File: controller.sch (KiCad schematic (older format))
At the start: 26 parts, among them J1 CONN_01X04, J2 CONN_01X02, J3 CONN_01X02, J4 CONN_01X02, J5 CONN_01X02, J6 CONN_01X02, U1 ATTINY13A-SU

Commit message: Make last changes
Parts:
- removed J4, J5: CONN_01X02, Connectors:PINHEAD1-2, symbol CONN_01X02
- added D4: D, symbol D
- added Q1: BF244A, TO_SOT_Packages_THT:TO-92_Molded_Narrow, symbol BF244A
- added Q?: IRLB8721PBF, TO_SOT_Packages_THT:TO-220_Vertical, symbol IRLB8721PBF
- added U2: TL072, symbol TL072
- C1: value 47uF -> 220u
- C6: value 220uF -> 470u
- R1, R3: value 220 -> 1K
- R5: value 3.3K -> 4.3K
- R6: value 1K -> 1.2K
- R7: value 10K -> 1K; footprint Resistors_SMD:R_1206 -> (none)
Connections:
- net +2V8: now also D4.1 (K), Q1.1 (D), Q?.3 (S); no longer C1.1, C2.1, DC1.4 (VIN), J3.2 (P2), L1.2
- net +5V: now also U2.8 (V+), U2.8 (V+)
- net GND: now also D1.1 (K), D2.1 (K), Q?.1 (G), U2.4 (V-), U2.4 (V-); no longer R1.2, R3.2, R7.1
- net miso: now also J6.2 (P2)
- net at R7.2, U1.2 (PB3(CLKI/ADC3/PCINT3)): no longer DC1.2 (EN)
- net at R1.1: now also D1.2 (A); no longer D1.1 (K)
- net at R3.1: now also D2.2 (A); no longer D2.1 (K)
- net mosi renamed RC
- net RC: now also U2.3 (+)
- net sck renamed GC
- net GC: now also U2.5 (+); no longer J6.2 (P2)
- new net: R1.2, U2.1, U2.2 (-)
- new net: R3.2, U2.6 (-), U2.7
- new net: Q1.2 (G), R7.1
- new net VCC: C1.1, C2.1, DC1.4 (VIN), L1.2, Q1.3 (S)
- new net VDD: D4.2 (A), J3.2 (P2), Q?.2 (D)
- no-connect marks 0 -> 1
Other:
- moved on the sheet: D1, D2, R1

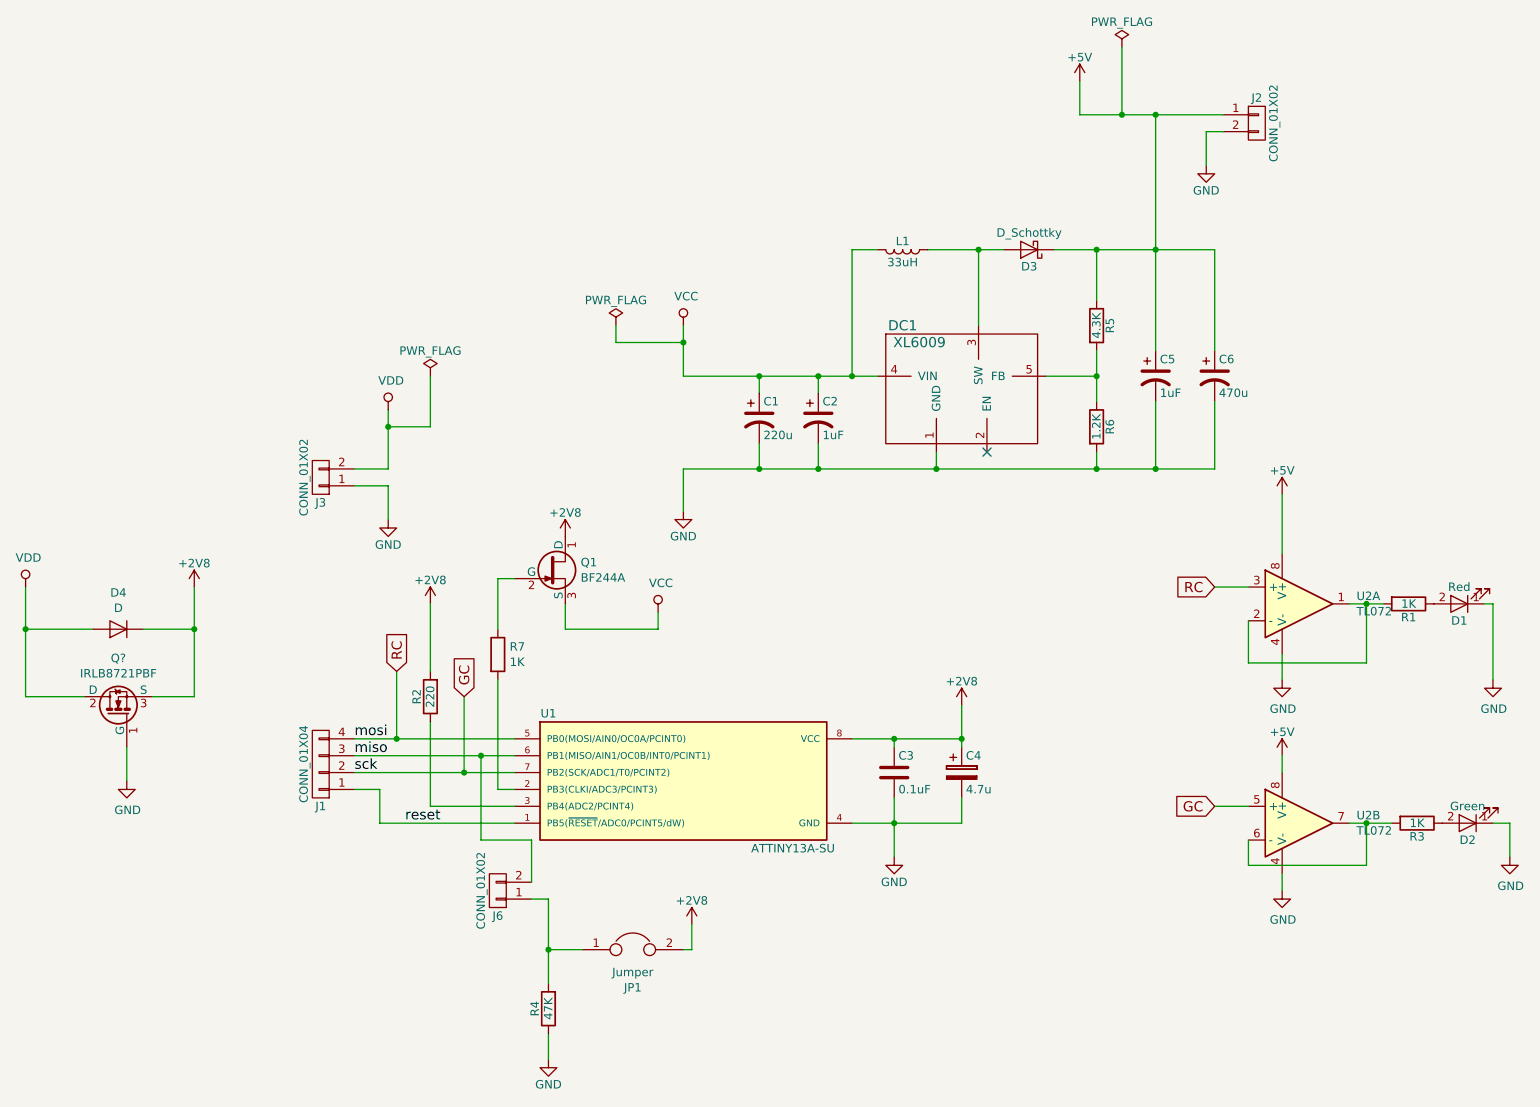
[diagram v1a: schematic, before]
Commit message: add circuit protection, refactor
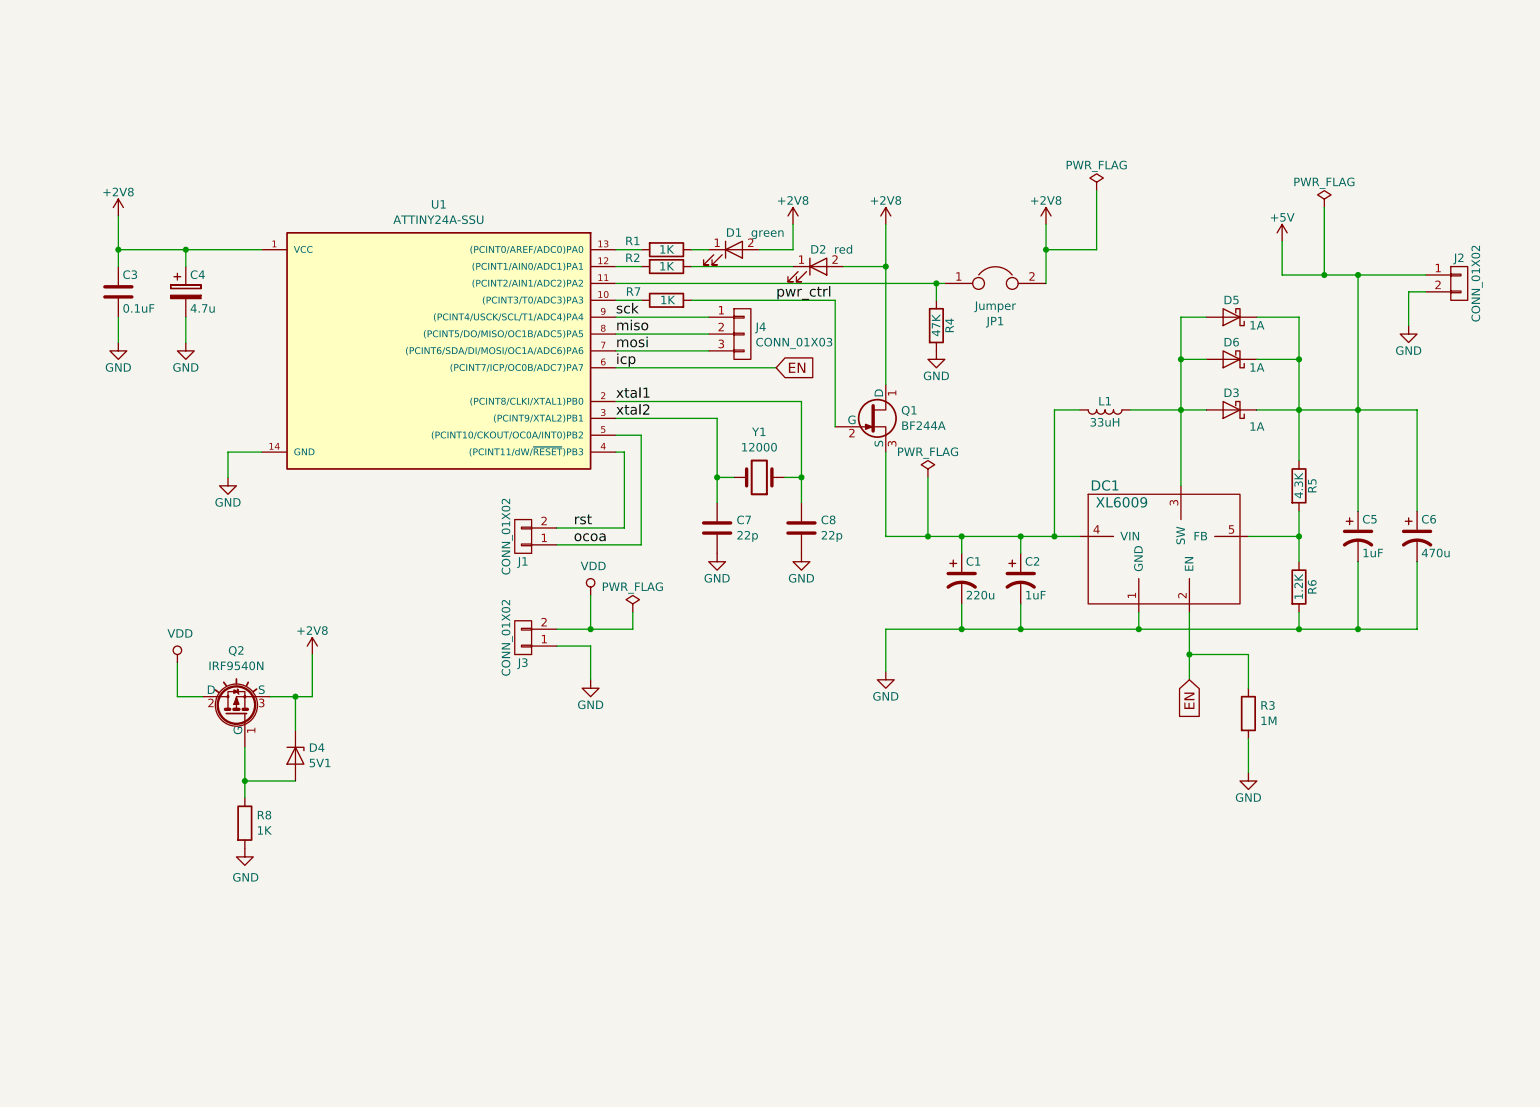
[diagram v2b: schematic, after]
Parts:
- removed D4: D, symbol D
- removed J1: CONN_01X04, Connectors_Molex:Molex_KK-6410-04_04x2.54mm_Straight, symbol CONN_01X04
- removed J6: CONN_01X02, Connectors:PINHEAD1-2, symbol CONN_01X02
- removed Q?: IRLB8721PBF, TO_SOT_Packages_THT:TO-220_Vertical, symbol IRLB8721PBF
- removed U1: ATTINY13A-SU, SMD_Packages:SOIC-8-N, symbol ATTINY13A-SU
- removed U2: TL072, symbol TL072
- added C7, C8: 22p, symbol C
- added D4: 5V1, symbol D_Zener_SOT23
- added D5, D6: 1A, Diodes_THT:D_DO-201_P12.70mm_Horizontal, symbol D_Schottky
- added J1: CONN_01X02, Connectors:PINHEAD1-2, symbol CONN_01X02
- added J4: CONN_01X03, symbol CONN_01X03
- added Q2: IRF9540N, TO_SOT_Packages_THT:TO-220_Vertical, symbol IRF9540N
- added R8: 1K, symbol R
- added U1: ATTINY24A-SSU, Housings_SOIC:SOIC-14_3.9x8.7mm_Pitch1.27mm, symbol ATTINY24A-SSU
- added Y1: 12000, symbol Crystal
- D1: value Red -> green
- D2: value Green -> red
- D3: value D_Schottky -> 1A
- R2: value 220 -> 1K
- R3: value 1K -> 1M; footprint Resistors_SMD:R_1206 -> (none)
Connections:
- net +2V8: now also D1.2 (A), D2.2 (A), D4.3 (K), Q2.3 (S), U1.1 (VCC); no longer R2.2
- net +5V: now also D5.1 (K), D6.1 (K)
- net GND: now also R3.2, R4.2, C7.2, C8.2, R8.2, U1.14 (GND); no longer D1.1 (K), D2.1 (K), R4.1
- net VDD: now also Q2.2 (D)
- net miso: now also J4.2 (P2), U1.8 ((PCINT5/DO/MISO/OC1B/ADC5)PA5)
- net EN: now reaches DC1.2 (EN)
- net EN: now also R3.1, U1.6 ((PCINT7/ICP/OC0B/ADC7)PA7)
- net at D3.2 (A), DC1.3 (SW), L1.1: now also D5.2 (A), D6.2 (A)
- net at R1.1: now also D1.1 (K); no longer D1.2 (A)
- net at R1.2: now also U1.13 ((PCINT0/AREF/ADC0)PA0)
- net pwr_ctrl: now reaches R7.2
- net pwr_ctrl: now also Q1.2 (G)
- net at R2.1: now also D2.1 (K)
- net at JP1.1: now also R4.1, U1.11 ((PCINT2/AIN1/ADC2)PA2); no longer R4.2
- net at R7.1: now also U1.10 ((PCINT3/T0/ADC3)PA3); no longer Q1.2 (G)
- net VCC: no longer names the net of C1.1, C2.1, DC1.4 (VIN), L1.2, Q1.3 (S)
- new net: R2.2, U1.12 ((PCINT1/AIN0/ADC1)PA1)
- new net: D4.1 (A), Q2.1 (G), R8.1
- new net mosi: J4.3 (P3), U1.7 ((PCINT6/SDA/DI/MOSI/OC1A/ADC6)PA6)
- new net ocoa: J1.1 (P1), U1.5 ((PCINT10/CKOUT/OC0A/INT0)PB2)
- new net rst: J1.2 (P2), U1.4 ((PCINT11/dW/~RESET~)PB3)
- new net sck: J4.1 (P1), U1.9 ((PCINT4/USCK/SCL/T1/ADC4)PA4)
- new net xtal1: C8.1, U1.2 ((PCINT8/CLKI/XTAL1)PB0), Y1.1
- new net xtal2: C7.1, U1.3 ((PCINT9/XTAL2)PB1), Y1.2
- no-connect marks 1 -> 0
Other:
- moved on the sheet: C1, C2, C4, C5, C6, D1, D3, DC1, J2, J3, L1, Q1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

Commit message: Remove ocsillators, add aref connection and pin for voltage check
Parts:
- removed C8: 22p, symbol C
- removed Y1: 12000, symbol Crystal
- added R9: 670K, Resistors_SMD:R_1206, symbol R
- C7: value 22p -> C
- J1: footprint Connectors:PINHEAD1-2 -> (none)
- J4: value CONN_01X03 -> SPI
- R3: footprint (none) -> Resistors_SMD:R_1206
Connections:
- net xtal1 is gone; now on an unnamed net: U1.2 ((PCINT8/CLKI/XTAL1)PB0)
- net +2V8: now also U1.12 ((PCINT1/AIN0/ADC1)PA1), R9.1
- net GND: now also C7.1, R9.2; no longer C7.2
- net at R1.2: now also U1.3 ((PCINT9/XTAL2)PB1); no longer U1.13 ((PCINT0/AREF/ADC0)PA0)
- net at R2.2: no longer U1.12 ((PCINT1/AIN0/ADC1)PA1)
- net ocoa: no longer names the net of J1.1 (P1), U1.5 ((PCINT10/CKOUT/OC0A/INT0)PB2)
- removed net xtal2: C7.1, U1.3 ((PCINT9/XTAL2)PB1)
- new net: C7.2, U1.13 ((PCINT0/AREF/ADC0)PA0)
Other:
- moved on the sheet: D1, D2, J3, R1, R2

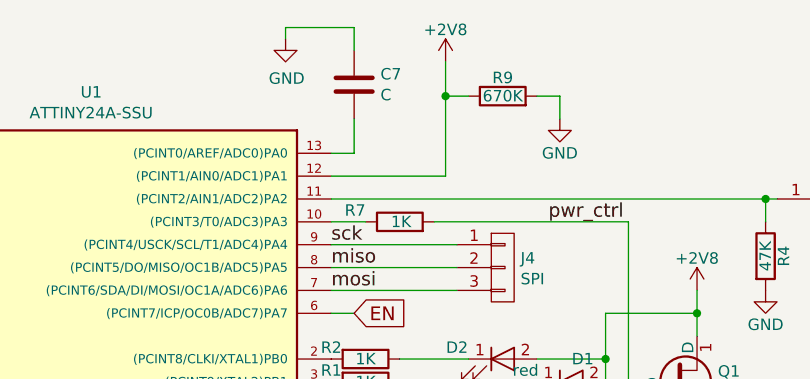
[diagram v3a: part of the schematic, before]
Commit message: Add capacitor value
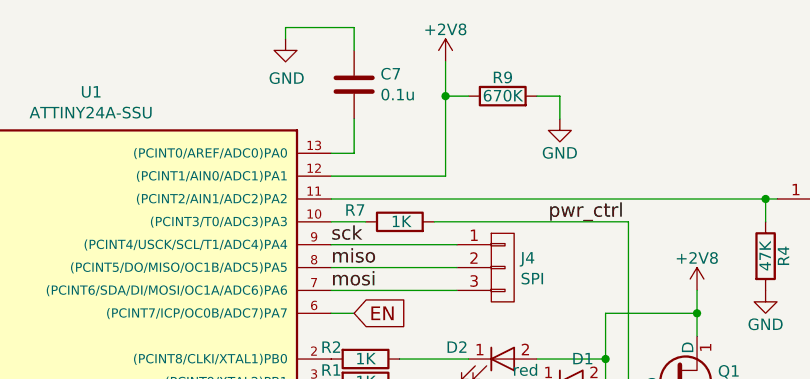
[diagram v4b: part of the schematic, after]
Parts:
- C7: value C -> 0.1u
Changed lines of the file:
@@
 Connection ~ 9350 3050
 $Comp
-L GND #PWR14
+L GND #PWR01
 U 1 1 58F22530
 P 6550 4600
-F 0 "#PWR14" H 6550 4350 50  0001 C CNN
+F 0 "#PWR01" H 6550 4350 50  0001 C CNN
 F 1 "GND" H 6550 4450 50  0000 C CNN
 F 2 "" H 6550 4600 50  0001 C CNN
@@
 	8900 2250 9750 2250
 $Comp
-L +5V #PWR18
+L +5V #PWR02
 U 1 1 58F23334
 P 8900 2050
-F 0 "#PWR18" H 8900 1900 50  0001 C CNN
+F 0 "#PWR02" H 8900 1900 50  0001 C CNN
 F 1 "+5V" H 8900 2190 50  0000 C CNN
 F 2 "" H 8900 2050 50  0001 C CNN
@@
 Connection ~ 9350 2250
 $Comp
-L GND #PWR19
+L GND #PWR03
 U 1 1 58F23494
 P 9650 2550
-F 0 "#PWR19" H 9650 2300 50  0001 C CNN
+F 0 "#PWR03" H 9650 2300 50  0001 C CNN
 F 1 "GND" H 9650 2400 50  0000 C CNN
 F 2 "" H 9650 2550 50  0001 C CNN
@@
 Connection ~ 8050 4350
 $Comp
-L PWR_FLAG #FLG4
+L PWR_FLAG #FLG04
 U 1 1 58F2B1AC
 P 9150 1850
-F 0 "#FLG4" H 9150 1925 50  0001 C CNN
+F 0 "#FLG04" H 9150 1925 50  0001 C CNN
 F 1 "PWR_FLAG" H 9150 2000 50  0000 C CNN
 F 2 "" H 9150 1850 50  0001 C CNN
@@
 	4050 5000 4500 5000
 $Comp
-L GND #PWR9
+L GND #PWR05
 U 1 1 58F2DC5B
 P 4250 5300
-F 0 "#PWR9" H 4250 5050 50  0001 C CNN
+F 0 "#PWR05" H 4250 5050 50  0001 C CNN
 F 1 "GND" H 4250 5150 50  0000 C CNN
 F 2 "" H 4250 5300 50  0001 C CNN
@@
 $EndComp
 $Comp
-L +2V8 #PWR16
+L +2V8 #PWR06
 U 1 1 592B3D9B
 P 7500 1950
-F 0 "#PWR16" H 7500 1800 50  0001 C CNN
+F 0 "#PWR06" H 7500 1800 50  0001 C CNN
 F 1 "+2V8" H 7500 2090 50  0000 C CNN
 F 2 "" H 7500 1950 50  0001 C CNN
@@
 $EndComp
 $Comp
-L PWR_FLAG #FLG2
+L PWR_FLAG #FLG07
 U 1 1 592D3FE0
 P 4500 4900
-F 0 "#FLG2" H 4500 4975 50  0001 C CNN
+F 0 "#FLG07" H 4500 4975 50  0001 C CNN
 F 1 "PWR_FLAG" H 4500 5050 50  0000 C CNN
 F 2 "" H 4500 4900 50  0001 C CNN
@@
 $EndComp
 $Comp
-L +2V8 #PWR7
+L +2V8 #PWR08
 U 1 1 592D4CFB
 P 3150 4500
-F 0 "#PWR7" H 3150 4350 50  0001 C CNN
+F 0 "#PWR08" H 3150 4350 50  0001 C CNN
 F 1 "+2V8" H 3150 4640 50  0000 C CNN
 F 2 "" H 3150 4500 50  0001 C CNN
@@
 $EndComp
 $Comp
-L GND #PWR6
+L GND #PWR09
 U 1 1 592D55AC
 P 2750 5650
-F 0 "#PWR6" H 2750 5400 50  0001 C CNN
+F 0 "#PWR09" H 2750 5400 50  0001 C CNN
 F 1 "GND" H 2755 5477 50  0000 C CNN
 F 2 "" H 2750 5650 50  0001 C CNN
@@
 $EndComp
 $Comp
-L VDD #PWR8
+L VDD #PWR010
 U 1 1 592D58A6
 P 4250 4800
-F 0 "#PWR8" H 4250 4650 50  0001 C CNN
+F 0 "#PWR010" H 4250 4650 50  0001 C CNN
 F 1 "VDD" H 4267 4973 50  0000 C CNN
 F 2 "" H 4250 4800 50  0001 C CNN
@@
 $EndComp
 $Comp
-L VDD #PWR3
+L VDD #PWR011
 U 1 1 592D5D4B
 P 2350 4550
-F 0 "#PWR3" H 2350 4400 50  0001 C CNN
+F 0 "#PWR011" H 2350 4400 50  0001 C CNN
 F 1 "VDD" H 2367 4723 50  0000 C CNN
 F 2 "" H 2350 4550 50  0001 C CNN
@@
 	2000 2100 2850 2100
 $Comp
-L GND #PWR5
+L GND #PWR012
 U 1 1 5932EF34
 P 2650 3450
-F 0 "#PWR5" H 2650 3200 50  0001 C CNN
+F 0 "#PWR012" H 2650 3200 50  0001 C CNN
 F 1 "GND" H 2650 3300 50  0000 C CNN
 F 2 "" H 2650 3450 50  0001 C CNN
@@
 $EndComp
 $Comp
-L +2V8 #PWR13
+L +2V8 #PWR013
 U 1 1 593325FC
 P 6550 2700
-F 0 "#PWR13" H 6550 2550 50  0001 C CNN
+F 0 "#PWR013" H 6550 2550 50  0001 C CNN
 F 1 "+2V8" H 6550 2840 50  0000 C CNN
 F 2 "" H 6550 2700 50  0001 C CNN
@@
 $EndComp
 $Comp
-L GND #PWR15
+L GND #PWR014
 U 1 1 5933473B
 P 6850 2700
-F 0 "#PWR15" H 6850 2450 50  0001 C CNN
+F 0 "#PWR014" H 6850 2450 50  0001 C CNN
 F 1 "GND" H 6850 2550 50  0000 C CNN
 F 2 "" H 6850 2700 50  0001 C CNN
@@
 $EndComp
 $Comp
-L +2V8 #PWR1
+L +2V8 #PWR015
 U 1 1 59341595
 P 2000 1900
-F 0 "#PWR1" H 2000 1750 50  0001 C CNN
+F 0 "#PWR015" H 2000 1750 50  0001 C CNN
 F 1 "+2V8" H 2000 2040 50  0000 C CNN
 F 2 "" H 2000 1900 50  0001 C CNN
@@
 Connection ~ 2000 2100
 $Comp
-L GND #PWR2
+L GND #PWR016
 U 1 1 59341A81
 P 2000 2650
-F 0 "#PWR2" H 2000 2400 50  0001 C CNN
+F 0 "#PWR016" H 2000 2400 50  0001 C CNN
 F 1 "GND" H 2000 2500 50  0000 C CNN
 F 2 "" H 2000 2650 50  0001 C CNN
@@
 $EndComp
 $Comp
-L GND #PWR4
+L GND #PWR017
 U 1 1 59341C3E
 P 2400 2650
-F 0 "#PWR4" H 2400 2400 50  0001 C CNN
+F 0 "#PWR017" H 2400 2400 50  0001 C CNN
 F 1 "GND" H 2400 2500 50  0000 C CNN
 F 2 "" H 2400 2650 50  0001 C CNN
@@
 $EndComp
 $Comp
-L GND #PWR17
+L GND #PWR018
 U 1 1 59343DED
 P 8700 5200
-F 0 "#PWR17" H 8700 4950 50  0001 C CNN
+F 0 "#PWR018" H 8700 4950 50  0001 C CNN
 F 1 "GND" H 8700 5050 50  0000 C CNN
 F 2 "" H 8700 5200 50  0001 C CNN
@@
 	6550 3300 6550 3800
 $Comp
-L PWR_FLAG #FLG3
+L PWR_FLAG #FLG019
 U 1 1 593471A3
 P 6800 3450
-F 0 "#FLG3" H 6800 3525 50  0001 C CNN
+F 0 "#FLG019" H 6800 3525 50  0001 C CNN
 F 1 "PWR_FLAG" H 6800 3600 50  0000 C CNN
 F 2 "" H 6800 3450 50  0001 C CNN
@@
 rst
 $Comp
-L +2V8 #PWR11
+L +2V8 #PWR020
 U 1 1 593C5363
 P 5450 1700
-F 0 "#PWR11" H 5450 1550 50  0001 C CNN
+F 0 "#PWR020" H 5450 1550 50  0001 C CNN
 F 1 "+2V8" H 5450 1840 50  0000 C CNN
 F 2 "" H 5450 1700 50  0001 C CNN
@@
 $EndComp
 $Comp
-L GND #PWR12
+L GND #PWR021
 U 1 1 593C5E5C
 P 5950 1950
-F 0 "#PWR12" H 5950 1700 50  0001 C CNN
+F 0 "#PWR021" H 5950 1700 50  0001 C CNN
 F 1 "GND" H 5950 1800 50  0000 C CNN
 F 2 "" H 5950 1950 50  0001 C CNN
@@
 $EndComp
 $Comp
-L PWR_FLAG #FLG1
+L PWR_FLAG #FLG022
 U 1 1 593CBD3E
 P 3450 4250
-F 0 "#FLG1" H 3450 4325 50  0001 C CNN
+F 0 "#FLG022" H 3450 4325 50  0001 C CNN
 F 1 "PWR_FLAG" H 3450 4400 50  0000 C CNN
 F 2 "" H 3450 4250 50  0001 C CNN
@@
 P 5050 1800
 F 0 "C7" H 5165 1846 50  0000 L CNN
-F 1 "C" H 5165 1755 50  0000 L CNN
+F 1 "0.1u" H 5165 1755 50  0000 L CNN
 F 2 "" H 5088 1650 50  0001 C CNN
 F 3 "" H 5050 1800 50  0001 C CNN
@@
 $EndComp
 $Comp
-L GND #PWR10
+L GND #PWR023
 U 1 1 593CEE71
 P 4750 1600
-F 0 "#PWR10" H 4750 1350 50  0001 C CNN
+F 0 "#PWR023" H 4750 1350 50  0001 C CNN
 F 1 "GND" H 4755 1427 50  0000 C CNN
 F 2 "" H 4750 1600 50  0001 C CNN

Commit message: Save changes
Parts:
- removed D5, D6: 1A, Diodes_THT:D_DO-201_P12.70mm_Horizontal, symbol D_Schottky
- added C8: 220u, Capacitors_SMD:CP_Elec_5x5.3, symbol CP1
- added C9: 470u, Capacitors_Tantalum_SMD:CP_Tantalum_Case-V_EIA-7343-20_Hand, symbol CP1
- added R10: 1.5K, Resistors_SMD:R_1206, symbol R
- C2, C5: footprint Capacitors_SMD:C_1210 -> Capacitors_SMD:C_0805
- C7: footprint (none) -> Capacitors_SMD:C_0805
- D3: value 1A -> 5A
- J1: footprint (none) -> Connectors_Molex:Molex_KK-6410-02_02x2.54mm_Straight
- J2, J3: footprint Connectors:PINHEAD1-2 -> Connectors_Molex:Molex_KK-6410-02_02x2.54mm_Straight
- J4: footprint (none) -> Connectors_Molex:Molex_KK-6410-03_03x2.54mm_Straight
- R1, R2: value 1K -> 330
- R5: value 4.3K -> 3.6K
- R7, R8: footprint (none) -> Resistors_SMD:R_1206
- R9: value 670K -> 330
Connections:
- net +2V8: now also R10.1; no longer D1.2 (A), D2.2 (A), R9.1, U1.12 ((PCINT1/AIN0/ADC1)PA1)
- net +5V: now also C9.1
- net GND: now also R1.2, R2.2, C8.2, C9.2
- net at C1.1, C2.1, DC1.4 (VIN)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: now also C8.1
- net at U1.3 ((PCINT9/XTAL2)PB1): now also D2.2 (A); no longer R1.2
- net at U1.2 ((PCINT8/CLKI/XTAL1)PB0): now also D1.2 (A); no longer R2.2
- net ss: now reaches J1.1 (P1), U1.5 ((PCINT10/CKOUT/OC0A/INT0)PB2)
- new net: R10.2, R9.1, U1.12 ((PCINT1/AIN0/ADC1)PA1)
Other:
- moved on the sheet: D1, D2, R1, R2

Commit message: save changes
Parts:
- removed Q1: BF244A, TO_SOT_Packages_THT:TO-92_Molded_Narrow, symbol BF244A
- removed Q2: IRF9540N, TO_SOT_Packages_THT:TO-220_Vertical, symbol IRF9540N
- added Q1: AO3401A, TO_SOT_Packages_SMD:SOT-23, symbol AO3401A
- added Q2: AO3400A, TO_SOT_Packages_SMD:SOT-23, symbol AO3400A
- C1, C8: footprint Capacitors_SMD:CP_Elec_5x5.3 -> Capacitors_SMD:CP_Elec_6.3x7.7
- C4: footprint Capacitors_SMD:CP_Elec_5x5.3 -> Capacitors_SMD:CP_Elec_4x5.7
- D4: footprint (none) -> TO_SOT_Packages_SMD:SOT-23
- R1, R10, R2, R5, R6, R7, R8, R9: footprint Resistors_SMD:R_1206 -> Resistors_SMD:R_0805
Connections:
- net +2V8: now also Q1.2 (S), Q2.3 (D)
- net VDD: now also Q1.3 (D)
- net pwr_ctrl: now also Q2.1 (G)
- net at C1.1, C2.1, C8.1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: now also Q2.2 (S)
- net at D4.1 (A), R8.1: now also Q1.1 (G)

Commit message: Complete pcb
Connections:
- net green: now reaches D1.2 (A), U1.2 ((PCINT8/CLKI/XTAL1)PB0)
- net red: now reaches D2.2 (A), U1.3 ((PCINT9/XTAL2)PB1)
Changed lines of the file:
@@
 Wire Wire Line
 	3150 5250 2750 5250
+Text Label 5000 3000 0    60   ~ 0
+green
+Text Label 5000 3100 0    60   ~ 0
+red
+Text Label 2350 4750 0    60   ~ 0
+vdd
 $EndSCHEMATC

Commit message: change pcb
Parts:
- removed C7: 0.1u, Capacitors_SMD:C_0805, symbol C
- removed J4: SPI, Connectors_Molex:Molex_KK-6410-03_03x2.54mm_Straight, symbol CONN_01X03
- added J4: CONN_01X04, Connectors_Molex:Molex_KK-6410-04_04x2.54mm_Straight, symbol CONN_01X04
- added R11, R12, R13: 0, Resistors_SMD:R_2512, symbol R
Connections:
- net +2V8: now also R13.1, R13.2
- net EN: now also R11.2; no longer DC1.2 (EN), R3.1
- net GND: now also R12.1, R12.2
- net miso: now also J4.3 (P3)
- net mosi: now also J4.4 (P4)
- net sck: now also J4.2 (P2)
- net at JP1.1, R4.1: now also U1.12 ((PCINT1/AIN0/ADC1)PA1); no longer U1.11 ((PCINT2/AIN1/ADC2)PA2)
- net at R7.1: now also U1.13 ((PCINT0/AREF/ADC0)PA0); no longer U1.10 ((PCINT3/T0/ADC3)PA3)
- net at R10.2, R9.1: now also U1.11 ((PCINT2/AIN1/ADC2)PA2); no longer U1.12 ((PCINT1/AIN0/ADC1)PA1)
- net pwr_ctrl: no longer names the net of Q2.1 (G), R7.2
- new net: DC1.2 (EN), R11.1, R3.1
- new net: J4.1 (P1), U1.10 ((PCINT3/T0/ADC3)PA3)
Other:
- moved on the sheet: R7
